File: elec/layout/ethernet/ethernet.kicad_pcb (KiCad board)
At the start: 2 copper layers, 6 parts

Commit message: remove default build, build everything locally
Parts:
- removed C1: 16V 100nF X7R ±10% 0402 Multilayer Ceramic Capacitors MLCC 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, lib:C0402
- removed C2, C3: 25V 10uF X5R ±10% 0805 Multilayer Ceramic Capacitors MLCC -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, lib:C0805
- removed R1: 62.5mW Thick Film Resistors ±100ppm/℃ ±1% 10kΩ 0402 Chip Re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, lib:R0402
- added U1: 10nF ±10% 50V X7R, atopile:C0402-b3ef17, F.Cu at (80.0, -5.00)
- added U10: 12.4kΩ ±1% 62.5mW, atopile:R0402-56259e, F.Cu at (20.0, -5.00)
- added U11: 1nF ±10% 50V X7R, atopile:C0805-3b2e55, F.Cu at (10.0, -5.00)
- added U12: 220Ω ±1% 62.5mW, atopile:R0402-56259e, F.Cu at (90.0, -5.00)
- added U13: 1MΩ ±1% 62.5mW, atopile:R0402-56259e, F.Cu at (320.0, -5.00)
- added U14: , lib:CRYSTAL-SMD_4P-L3.2-W2.5-BL, F.Cu at (190.0, -5.00)
- added U15: 10pF ±5% 50V C0G, atopile:C0402-b3ef17, F.Cu at (250.0, -5.00)
- added U16: 10pF ±5% 50V C0G, atopile:C0402-b3ef17, F.Cu at (30.0, -5.00)
- added U17: , lib:RJ45-TH_J1B1211CCD, F.Cu at (130.0, -5.00)
- added U18: 10nF ±10% 50V X7R, atopile:C0402-b3ef17, F.Cu at (310.0, -5.00)
- added U19: 6.8nF ±10% 50V X7R, atopile:C0402-b3ef17, F.Cu at (140.0, -5.00)
- added U20: 33Ω ±1% 62.5mW, atopile:R0402-56259e, F.Cu at (110.0, -5.00)
- added U21: 49.9Ω ±1% 62.5mW, atopile:R0402-56259e, F.Cu at (240.0, -5.00)
- added U22: 6.8nF ±10% 50V X7R, atopile:C0402-b3ef17, F.Cu at (200.0, -5.00)
- added U23: 33Ω ±1% 62.5mW, atopile:R0402-56259e, F.Cu at (290.0, -5.00)
- added U24: 49.9Ω ±1% 62.5mW, atopile:R0402-56259e, F.Cu at (60.0, -5.00)
- added U25: 4.7µF ±10% 10V X5R, atopile:C0402-b3ef17, F.Cu at (280.0, -5.00)
- added U26: 22nF ±10% 50V X7R, atopile:C0402-b3ef17, F.Cu at (50.0, -5.00)
- added U27: 10Ω ±1% 62.5mW, atopile:R0402-56259e, F.Cu at (70.0, -5.00)
- added U28: 33Ω ±1% 62.5mW, atopile:R0402-56259e, F.Cu at (300.0, -5.00)
- added U29: 49.9Ω ±1% 62.5mW, atopile:R0402-56259e, F.Cu at (260.0, -5.00)
- added U3: 10µF ±10% 25V X5R, atopile:C0805-3b2e55, F.Cu at (270.0, -5.00)
- added U30: 33Ω ±1% 62.5mW, atopile:R0402-56259e, F.Cu at (100.0, -5.00)
- added U31: 49.9Ω ±1% 62.5mW, atopile:R0402-56259e, F.Cu at (150.0, -5.00)
- added U32: , lib:LQFP-48_L7.0-W7.0-P0.50-LS9.0-BL, F.Cu at (210.0, -5.00)
- added U4: 100nF ±10% 16V X7R, atopile:C0402-b3ef17, F.Cu at (120.0, -5.00)
- added U5: 100nF ±10% 16V X7R, atopile:C0402-b3ef17, F.Cu at (170.0, -5.00)
- added U6: 100nF ±10% 16V X7R, atopile:C0402-b3ef17, F.Cu at (40.0, -5.00)
- added U7: 100nF ±10% 16V X7R, atopile:C0402-b3ef17, F.Cu at (160.0, -5.00)
- added U8: 100nF ±10% 16V X7R, atopile:C0402-b3ef17, F.Cu at (180.0, -5.00)
- added U9: 100nF ±10% 16V X7R, atopile:C0402-b3ef17, F.Cu at (230.0, -5.00)
- U2: value (none) -> 220Ω ±1% 62.5mW; footprint lib:KEY-SMD_4P-L4.2-W3.2-P2.20-LS4.6 -> atopile:R0402-56259e
- moved U2 150.6 mm to (220.0, -5.00), turned to 0 degrees
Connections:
- U1 pad 11: io18 -> (no net)
- U1 pad 12: io8 -> (no net)
- U1 pad 13: io19 -> (no net)
- U1 pad 15: io3 -> (no net)
- U1 pad 16: io46 -> (no net)
- U1 pad 17: io9 -> (no net)
- U1 pad 19: io11 -> (no net)
- U1 pad 2: vcc -> (no net)
- U1 pad 20: io12 -> (no net)
- U1 pad 21: io13 -> (no net)
- U1 pad 23: io21 -> (no net)
- U1 pad 24: io47 -> (no net)
- U1 pad 25: io48 -> (no net)
- U1 pad 27: io0 -> (no net)
- U1 pad 28: io35 -> (no net)
- U1 pad 29: io36 -> (no net)
- U1 pad 3: en -> (no net)
- U1 pad 31: io38 -> (no net)
- U1 pad 32: io39 -> (no net)
- U1 pad 33: io40 -> (no net)
- U1 pad 34: io41 -> (no net)
- U1 pad 35: io42 -> (no net)
- U1 pad 37: txd0 -> (no net)
- U1 pad 38: io2 -> (no net)
- U1 pad 39: io1 -> (no net)
- U1 pad 4: io4 -> (no net)
- U1 pad 5: io5 -> (no net)
- U1 pad 7: io7 -> (no net)
- U1 pad 8: io15 -> (no net)
- U1 pad 9: io16 -> (no net)
- U2 pad 1: en -> ACTLED
- U2 pad 2: en -> RLED_minus
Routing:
- net (no net): track 0.00 -> 15.5 mm
- net en: track 8.40 -> 0.00 mm
- net vcc: track 7.15 -> 0.00 mm

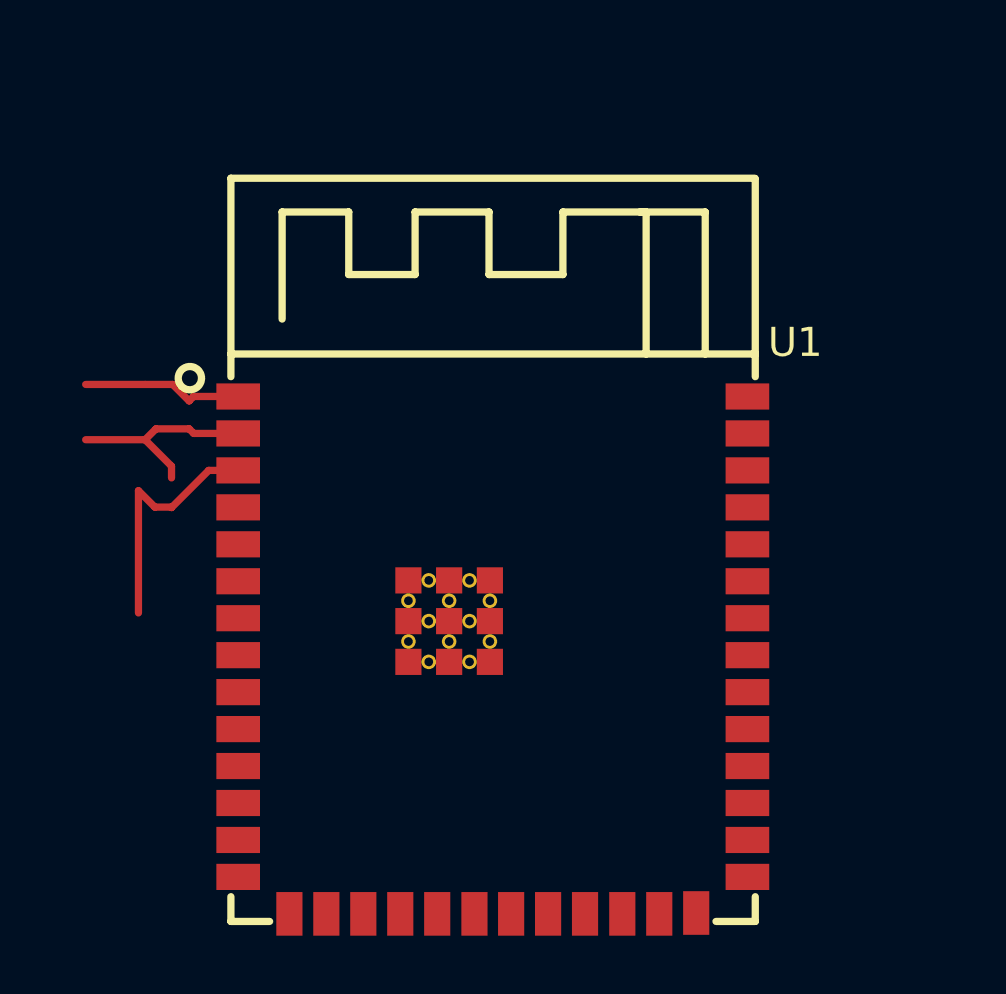
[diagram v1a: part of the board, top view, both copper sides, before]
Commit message: add module builds back in to ato.yaml with mfg-data excluded in config
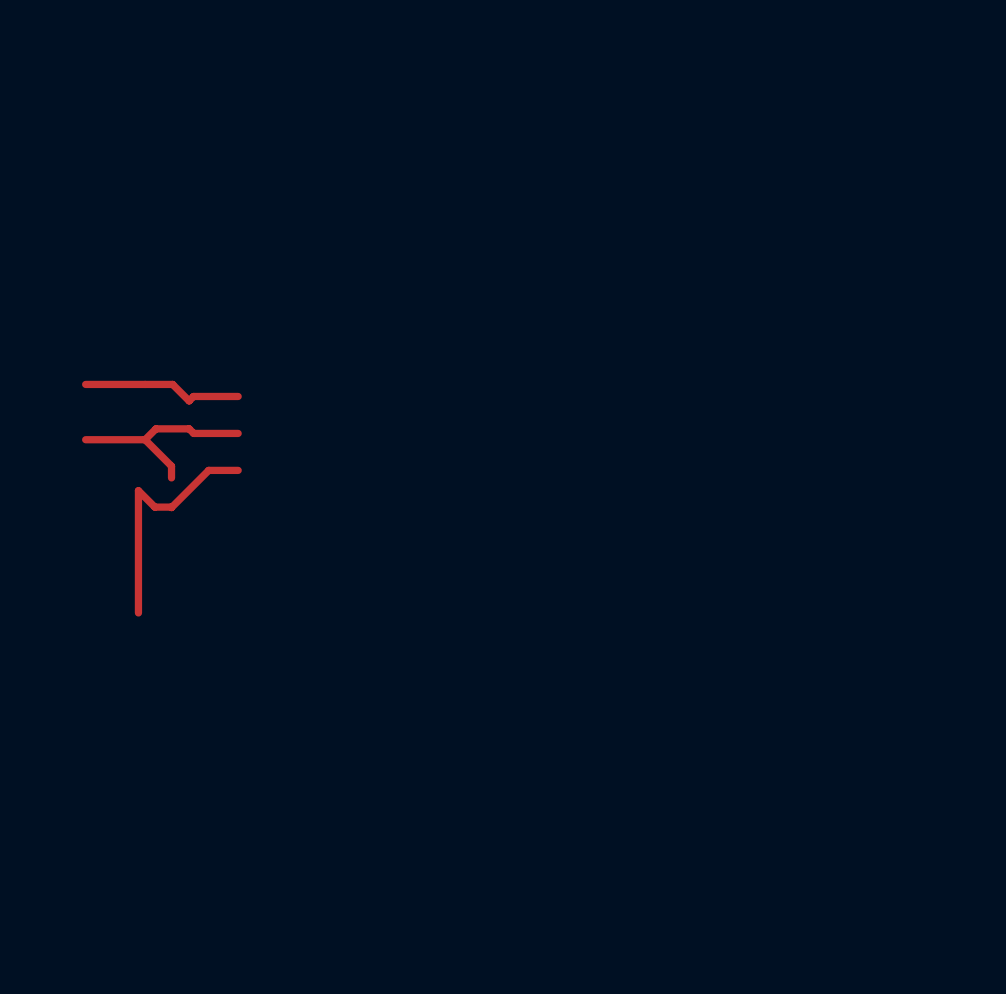
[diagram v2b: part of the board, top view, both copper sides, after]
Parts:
- removed the U1 at (114.4, 90.9)
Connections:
- net RLED_plus renamed AVDD
- net sck renamed SCLK
- U19 pad 1: net-1 -> net
- U20 pad 2: net-1 -> net
- U22 pad 1: net -> net-1
- U23 pad 2: net -> net-1

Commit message: update ethernet layout
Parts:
- removed U10: 12.4kΩ ±1% 62.5mW, atopile:R0402-56259e
- removed U11: 1nF ±10% 50V X7R, atopile:C0805-3b2e55
- removed U12: 220Ω ±1% 62.5mW, atopile:R0402-56259e
- removed U13: 1MΩ ±1% 62.5mW, atopile:R0402-56259e
- removed U14: , lib:CRYSTAL-SMD_4P-L3.2-W2.5-BL
- removed U15, U16: 10pF ±5% 50V C0G, atopile:C0402-b3ef17
- removed U17: , lib:RJ45-TH_J1B1211CCD
- removed U18: 10nF ±10% 50V X7R, atopile:C0402-b3ef17
- removed U19, U22: 6.8nF ±10% 50V X7R, atopile:C0402-b3ef17
- removed U20, U23, U28, U30: 33Ω ±1% 62.5mW, atopile:R0402-56259e
- removed U21, U24, U29, U31: 49.9Ω ±1% 62.5mW, atopile:R0402-56259e
- removed U25: 4.7µF ±10% 10V X5R, atopile:C0402-b3ef17
- removed U26: 22nF ±10% 50V X7R, atopile:C0402-b3ef17
- removed U27: 10Ω ±1% 62.5mW, atopile:R0402-56259e
- removed U32: , lib:LQFP-48_L7.0-W7.0-P0.50-LS9.0-BL
- removed U4, U5, U6, U7, U8, U9: 100nF ±10% 16V X7R, atopile:C0402-b3ef17
- added C1: 1nF ±10% 50V X7R, atopile:C0805-3b2e55, F.Cu at (103.3, 73.6)
- added C10: 100nF ±10% 16V X7R, atopile:C0402-b3ef17, F.Cu at (112.0, 74.2)
- added C11: 100nF ±10% 16V X7R, atopile:C0402-b3ef17, F.Cu at (114.2, 61.1)
- added C12: 100nF ±10% 16V X7R, atopile:C0402-b3ef17, F.Cu at (112.2, 61.1)
- added C13: 100nF ±10% 16V X7R, atopile:C0402-b3ef17, F.Cu at (114.0, 74.2)
- added C14: 10µF ±10% 25V X5R, atopile:C0805-3b2e55, F.Cu at (110.0, 61.0)
- added C15: 10pF ±5% 50V C0G, atopile:C0402-b3ef17, F.Cu at (123.1, 68.8)
- added C16: 10pF ±5% 50V C0G, atopile:C0402-b3ef17, F.Cu at (124.8, 66.3)
- added C2: 22nF ±10% 50V X7R, atopile:C0402-b3ef17, F.Cu at (101.6, 60.7)
- added C3: 6.8nF ±10% 50V X7R, atopile:C0402-b3ef17, F.Cu at (101.6, 69.8)
- added C4: 6.8nF ±10% 50V X7R, atopile:C0402-b3ef17, F.Cu at (101.6, 66.6)
- added C5: 10nF ±10% 50V X7R, atopile:C0402-b3ef17, F.Cu at (103.6, 67.5)
- added C6: 10nF ±10% 50V X7R, atopile:C0402-b3ef17, F.Cu at (115.0, 74.2)
- added C7: 4.7µF ±10% 10V X5R, atopile:C0402-b3ef17, F.Cu at (113.0, 74.2)
- added C8: 100nF ±10% 16V X7R, atopile:C0402-b3ef17, F.Cu at (113.2, 61.1)
- added C9: 100nF ±10% 16V X7R, atopile:C0402-b3ef17, F.Cu at (111.0, 74.2)
- added R1: 220Ω ±1% 62.5mW, atopile:R0402-56259e, F.Cu at (119.0, 70.4)
- added R10: 49.9Ω ±1% 62.5mW, atopile:R0402-56259e, F.Cu at (101.6, 68.7)
- added R11: 49.9Ω ±1% 62.5mW, atopile:R0402-56259e, F.Cu at (101.6, 67.6)
- added R12: 12.4kΩ ±1% 62.5mW, atopile:R0402-56259e, F.Cu at (106.9, 69.1)
- added R13: 1MΩ ±1% 62.5mW, atopile:R0402-56259e, F.Cu at (124.8, 68.4)
- added R2: 220Ω ±1% 62.5mW, atopile:R0402-56259e, F.Cu at (119.0, 69.4)
- added R3: 33Ω ±1% 62.5mW, atopile:R0402-56259e, F.Cu at (101.6, 62.9)
- added R4: 33Ω ±1% 62.5mW, atopile:R0402-56259e, F.Cu at (105.9, 64.5)
- added R5: 49.9Ω ±1% 62.5mW, atopile:R0402-56259e, F.Cu at (101.6, 61.9)
- added R6: 49.9Ω ±1% 62.5mW, atopile:R0402-56259e, F.Cu at (101.6, 65.6)
- added R7: 10Ω ±1% 62.5mW, atopile:R0402-56259e, F.Cu at (101.6, 63.9)
- added R8: 33Ω ±1% 62.5mW, atopile:R0402-56259e, F.Cu at (103.4, 69.7)
- added R9: 33Ω ±1% 62.5mW, atopile:R0402-56259e, F.Cu at (103.5, 66.6)
- U1: value 10nF ±10% 50V X7R -> (none); footprint atopile:C0402-b3ef17 -> lib:LQFP-48_L7.0-W7.0-P0.50-LS9.0-BL
- U2: value 220Ω ±1% 62.5mW -> (none); footprint atopile:R0402-56259e -> lib:RJ45-TH_J1B1211CCD
- U3: value 10µF ±10% 25V X5R -> (none); footprint atopile:C0805-3b2e55 -> lib:CRYSTAL-SMD_4P-L3.2-W2.5-BL
- moved U3 164.1 mm to (122.2, 66.4)
- moved U2 147.3 mm to (91.6, 67.3), turned to -90 degrees
- moved U1 79.6 mm to (112.8, 67.5), turned to -90 degrees
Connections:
- U1 pad 1: _1V2O -> TXN
- U1 pad 2: gnd -> TXP
- U2 pad 1: ACTLED -> TD_plus
- U2 pad 2: RLED_minus -> TCT
- U3 pad 1: AVDD -> xin
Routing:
- net AVDD: track 0.00 -> 41.7 mm, vias 0 -> 8
- net LLED_minus: track 0.00 -> 41.5 mm, vias 0 -> 1
- net RLED_minus: track 0.00 -> 39.9 mm, vias 0 -> 1
- net CGND: track 0.00 -> 27.5 mm
- net gnd: track 0.00 -> 25.2 mm, vias 0 -> 8
- net (no net): track 15.5 -> 0.00 mm
- net TCT: track 0.00 -> 14.3 mm
- net xout: track 0.00 -> 13.1 mm
- net TD_minus: track 0.00 -> 11.0 mm, vias 0 -> 2
- net xin: track 0.00 -> 9.44 mm
- net RCT: track 0.00 -> 7.88 mm
- net TXP: track 0.00 -> 7.40 mm
- net RXN: track 0.00 -> 6.82 mm, vias 0 -> 2
- net TD_plus: track 0.00 -> 6.01 mm
- net ic-gnd: track 5.54 -> 0.00 mm
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
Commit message: rebuild all modules
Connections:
- net AVDD renamed LLED_plus
- U1 pad 23: rsvd -> (no net)
- U1 pad 38: rsvd -> (no net)
- U1 pad 39: rsvd -> (no net)
- U1 pad 40: rsvd -> (no net)
- U1 pad 41: rsvd -> (no net)
- U1 pad 42: rsvd -> (no net)

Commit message: core layout, rebuild modules with compiler updates
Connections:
- net LLED_plus renamed RLED_plus
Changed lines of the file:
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@@
     (net 1 "TCT")
     (net 2 "LLED_minus")
-    (net 3 "LLED_plus")
+    (net 3 "RLED_plus")
     (net 4 "RD_plus")
     (net 5 "RD_minus")
@@
             (layers "F.Cu" "F.Paste" "F.Mask")
             (remove_unused_layers no)
-            (net 3 "LLED_plus"))
+            (net 3 "RLED_plus"))
         (pad "2" smd rect
             (at 0.43 0 180)
@@
             (layers "F.Cu" "F.Paste" "F.Mask")
             (remove_unused_layers no)
-            (net 3 "LLED_plus"))
+            (net 3 "RLED_plus"))
         (pad "2" smd rect
             (at 0.55 0 90)
@@
             (layers "F.Cu" "F.Paste" "F.Mask")
             (remove_unused_layers no)
-            (net 3 "LLED_plus")
+            (net 3 "RLED_plus")
             (pintype "stereo"))
         (pad "5" smd oval
@@
             (layers "F.Cu" "F.Paste" "F.Mask")
             (remove_unused_layers no)
-            (net 3 "LLED_plus")
+            (net 3 "RLED_plus")
             (pintype "stereo"))
         (pad "9" smd oval
@@
             (layers "F.Cu" "F.Paste" "F.Mask")
             (remove_unused_layers no)
-            (net 3 "LLED_plus")
+            (net 3 "RLED_plus")
             (pintype "stereo"))
         (pad "12" smd oval
@@
             (layers "F.Cu" "F.Paste" "F.Mask")
             (remove_unused_layers no)
-            (net 3 "LLED_plus")
+            (net 3 "RLED_plus")
             (pintype "stereo"))
         (pad "16" smd oval
@@
             (layers "F.Cu" "F.Paste" "F.Mask")
             (remove_unused_layers no)
-            (net 3 "LLED_plus")
+            (net 3 "RLED_plus")
             (pintype "stereo"))
         (pad "18" smd oval
@@
             (layers "F.Cu" "F.Paste" "F.Mask")
             (remove_unused_layers no)
-            (net 3 "LLED_plus")
+            (net 3 "RLED_plus")
             (pintype "stereo"))
         (pad "22" smd oval
@@
             (layers "F.Cu" "F.Paste" "F.Mask")
             (remove_unused_layers no)
-            (net 3 "LLED_plus")
+            (net 3 "RLED_plus")
             (pintype "stereo"))
         (pad "29" smd oval
@@
             (layers "F.Cu" "F.Paste" "F.Mask")
             (remove_unused_layers no)
-            (net 3 "LLED_plus")
+            (net 3 "RLED_plus")
             (pintype "stereo"))
         (pad "44" smd oval
@@
             (layers "F.Cu" "F.Paste" "F.Mask")
             (remove_unused_layers no)
-            (net 3 "LLED_plus")
+            (net 3 "RLED_plus")
             (pintype "stereo"))
         (pad "45" smd oval
@@
             (layers "F.Cu" "F.Paste" "F.Mask")
             (remove_unused_layers no)
-            (net 3 "LLED_plus")
+            (net 3 "RLED_plus")
             (pintype "stereo"))
         (pad "46" smd oval
@@
             (layers "F.Cu" "F.Paste" "F.Mask")
             (remove_unused_layers no)
-            (net 3 "LLED_plus"))
+            (net 3 "RLED_plus"))
         (pad "2" smd rect
             (at 0.43 0 180)
@@
             (layers "*.Cu" "*.Mask")
             (remove_unused_layers no)
-            (net 3 "LLED_plus")
+            (net 3 "RLED_plus")
             (pintype "stereo"))
         (pad "11" thru_hole circle
@@
             (layers "*.Cu" "*.Mask")
             (remove_unused_layers no)
-            (net 3 "LLED_plus")
+            (net 3 "RLED_plus")
             (pintype "stereo"))
         (pad "13" thru_hole circle
@@
             (layers "F.Cu" "F.Paste" "F.Mask")
             (remove_unused_layers no)
-            (net 3 "LLED_plus"))
+            (net 3 "RLED_plus"))
         (pad "2" smd rect
             (at 0.55 0 270)
@@
             (layers "F.Cu" "F.Paste" "F.Mask")
             (remove_unused_layers no)
-            (net 3 "LLED_plus"))
+            (net 3 "RLED_plus"))
         (pad "2" smd rect
             (at 0.55 0 90)
@@
             (layers "F.Cu" "F.Paste" "F.Mask")
             (remove_unused_layers no)
-            (net 3 "LLED_plus"))
+            (net 3 "RLED_plus"))
         (pad "2" smd rect
             (at 0.43 0 180)
@@
             (layers "F.Cu" "F.Paste" "F.Mask")
             (remove_unused_layers no)
-            (net 3 "LLED_plus"))
+            (net 3 "RLED_plus"))
         (pad "2" smd rect
             (at 1 0 180)
@@
             (layers "F.Cu" "F.Paste" "F.Mask")
             (remove_unused_layers no)
-            (net 3 "LLED_plus"))
+            (net 3 "RLED_plus"))
         (pad "2" smd rect
             (at 0.55 0 270)
@@
             (layers "F.Cu" "F.Paste" "F.Mask")
             (remove_unused_layers no)
-            (net 3 "LLED_plus"))
+            (net 3 "RLED_plus"))
         (pad "2" smd rect
             (at 0.55 0 270)
@@
             (layers "F.Cu" "F.Paste" "F.Mask")
             (remove_unused_layers no)
-            (net 3 "LLED_plus"))
+            (net 3 "RLED_plus"))
         (pad "2" smd rect
             (at 0.55 0 90)
